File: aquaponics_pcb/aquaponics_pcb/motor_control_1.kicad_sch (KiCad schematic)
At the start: 1 part, among them IC4 DRV8214RTER

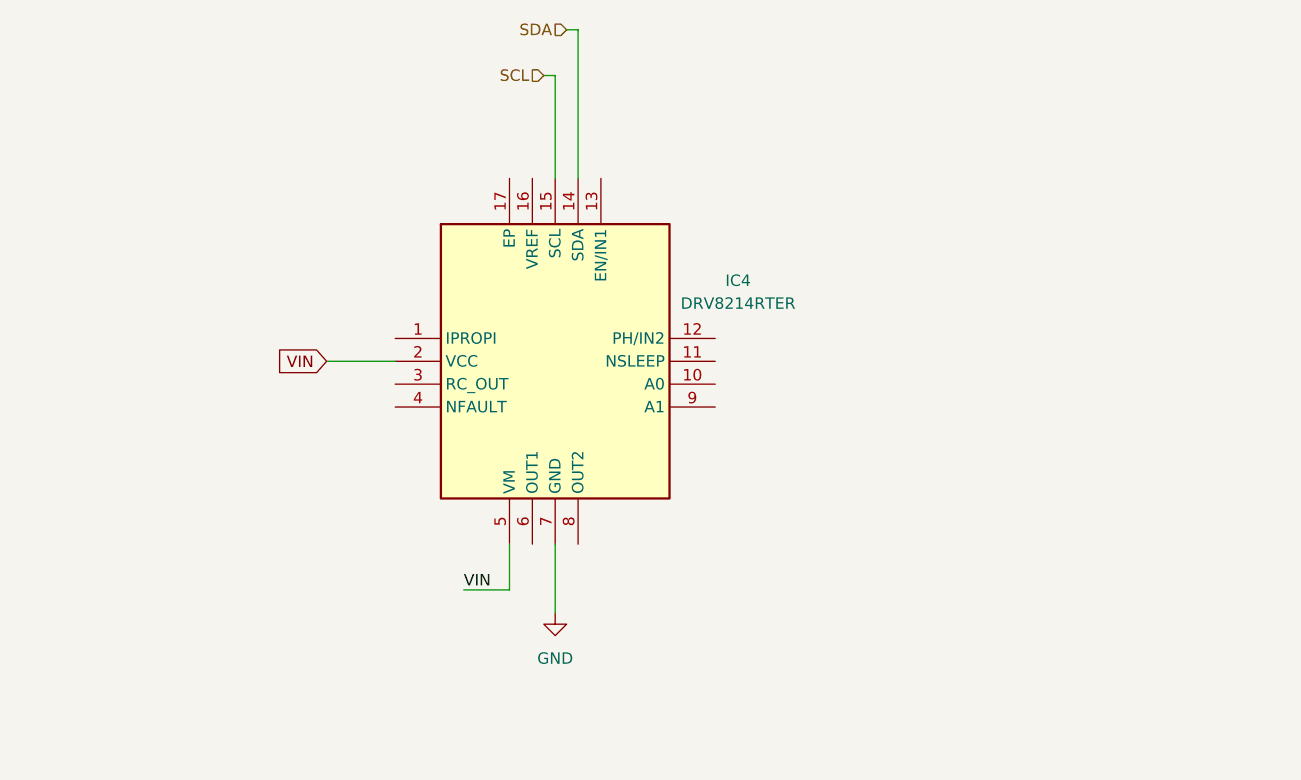
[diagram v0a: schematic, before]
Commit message: add ezo datasheets, update motor schematic and add 2 motors
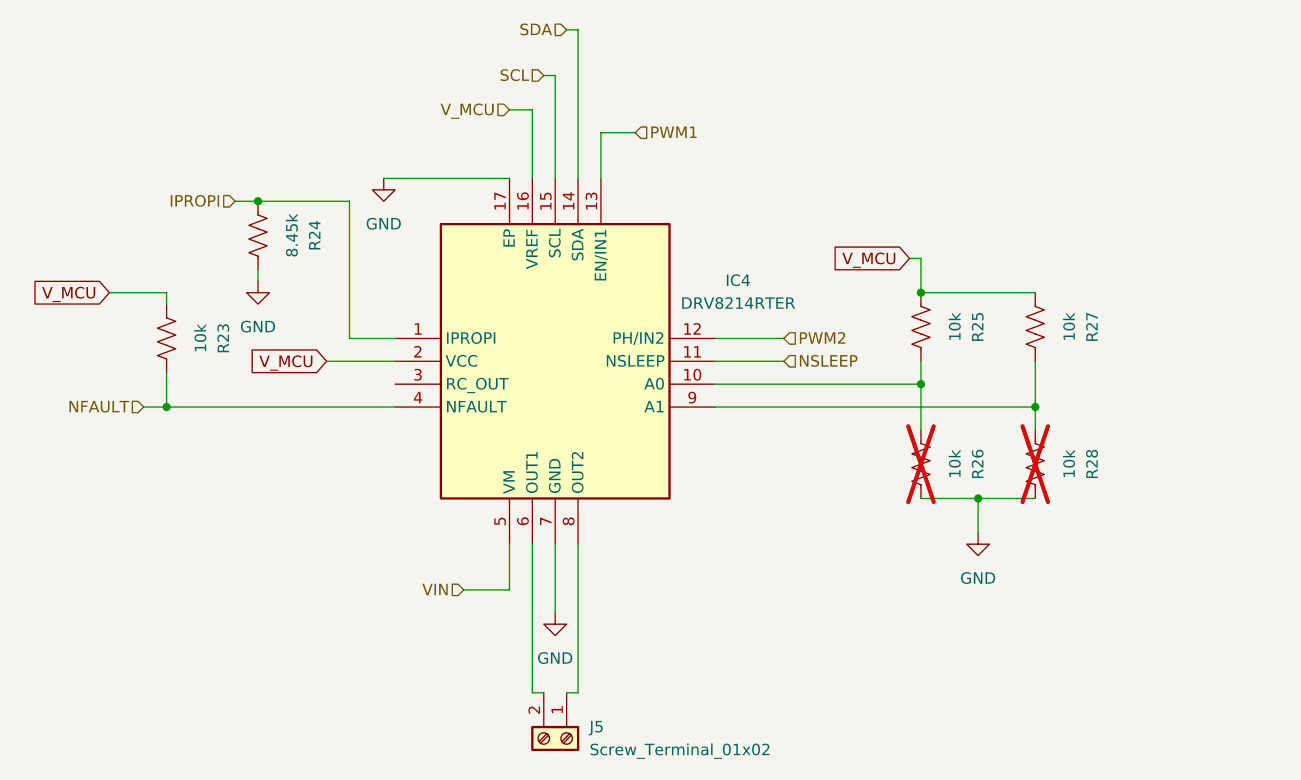
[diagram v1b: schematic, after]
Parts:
- added J5: Screw_Terminal_01x02, symbol Connector:Screw_Terminal_01x02
- added R23, R25, R26, R27, R28: 10k, Resistor_SMD:R_0603_1608Metric_Pad0.98x0.95mm_HandSolder, symbol Device:R_US
- added R24: 8.45k, Resistor_SMD:R_0603_1608Metric_Pad0.98x0.95mm_HandSolder, symbol Device:R_US
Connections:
- net GND: now also IC4.17 (EP), R24.2, R26.2, R28.2
- net VIN: no longer IC4.2 (VCC)
- net IPROPI: now reaches IC4.1 (IPROPI)
- net IPROPI: now also R24.1
- net at IC4.10 (A0): now also R25.2, R26.1
- net NSLEEP: now reaches IC4.11 (NSLEEP)
- net PWM2: now reaches IC4.12 (PH/IN2)
- net PWM1: now reaches IC4.13 (EN/IN1)
- net V_MCU: now reaches IC4.16 (VREF)
- net V_MCU: now also IC4.2 (VCC), R23.1, R25.1, R27.1
- net NFAULT: now reaches IC4.4 (NFAULT)
- net NFAULT: now also R23.2
- net at IC4.6 (OUT1): now also J5.2 (Pin_2)
- net at IC4.8 (OUT2): now also J5.1 (Pin_1)
- net at IC4.9 (A1): now also R27.2, R28.1

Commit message: add initial pcb layout
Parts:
- IC4: footprint QFN50P300X300X80-17N-D -> SamacSys_Parts:QFN50P300X300X80-17N-D
- J5: footprint (none) -> Connector_Phoenix_GMSTB:PhoenixContact_GMSTBA_2,5_2-G_1x02_P7.50mm_Horizontal
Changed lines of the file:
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@@
 			)
 		)
-		(property "Footprint" "QFN50P300X300X80-17N-D"
+		(property "Footprint" "SamacSys_Parts:QFN50P300X300X80-17N-D"
 			(at 153.67 171.12 0)
 			(effects
@@
 			)
 		)
-		(property "Footprint" ""
+		(property "Footprint" "Connector_Phoenix_GMSTB:PhoenixContact_GMSTBA_2,5_2-G_1x02_P7.50mm_Horizontal"
 			(at 140.97 130.81 0)
 			(effects

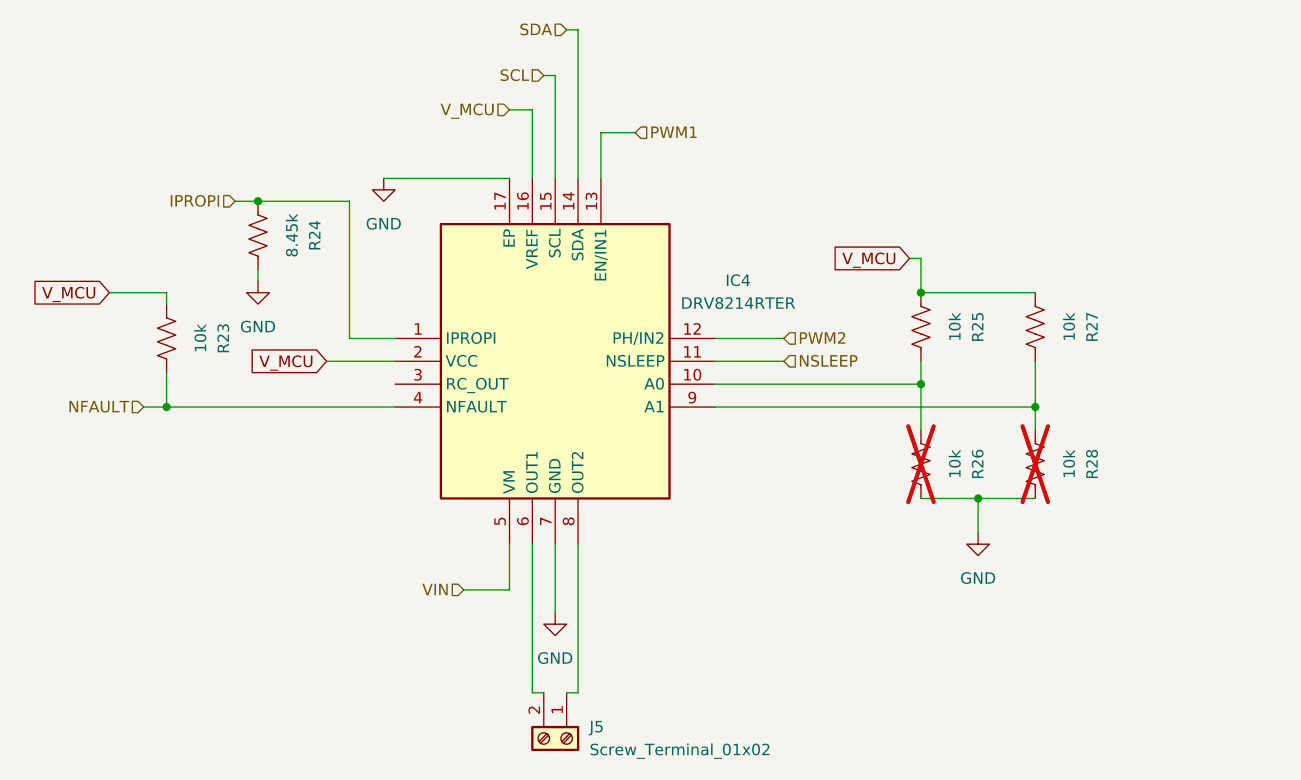
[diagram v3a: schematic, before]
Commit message: finish ground and power pours. fix rules and run final DRC. export gerbers
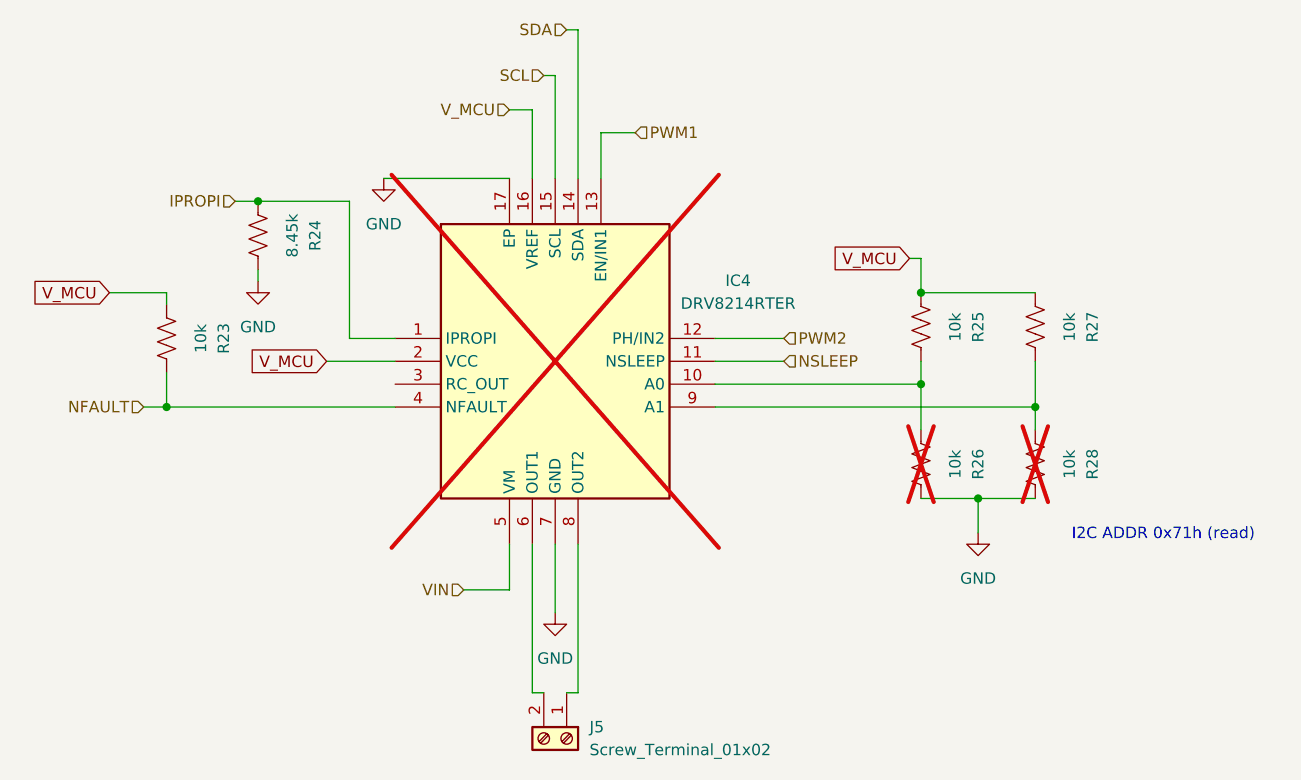
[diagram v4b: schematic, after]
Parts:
- IC4: now not fitted
- R23, R25, R27: JLCPCB Part # (none) -> C98220; LCSC Part Number (none) -> C98220
- R24: JLCPCB Part # (none) -> C2933263; LCSC Part Number (none) -> C2933263
- R26, R28: LCSC Part Number (none) -> C98220
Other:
- note added: "I2C ADDR 0x71h (read)"
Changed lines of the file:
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@@
 	(generator_version "9.0")
 	(paper "A4")
+	(text "I2C ADDR 0x71h (read)"
+		(exclude_from_sim no)
+		(at 207.264 108.204 0)
+		(effects
+			(font
+				(size 1.27 1.27)
+			)
+		)
+	)
 	(junction
 		(at 180.34 81.28)
@@
 		(property "Description" "Resistor, US symbol"
 			(at 180.34 85.09 0)
+			(effects
+				(font
+					(size 1.27 1.27)
+				)
+				(hide yes)
+			)
+		)
+		(property "LCSC Part Number" "C98220"
+			(at 180.34 85.09 90)
+			(effects
+				(font
+					(size 1.27 1.27)
+				)
+				(hide yes)
+			)
+		)
+		(property "JLCPCB Part #" "C98220"
+			(at 180.34 85.09 90)
 			(effects
 				(font
@@
 			)
 		)
+		(property "LCSC Part Number" "C98220"
+			(at 193.04 85.09 90)
+			(effects
+				(font
+					(size 1.27 1.27)
+				)
+				(hide yes)
+			)
+		)
+		(property "JLCPCB Part #" "C98220"
+			(at 193.04 85.09 90)
+			(effects
+				(font
+					(size 1.27 1.27)
+				)
+				(hide yes)
+			)
+		)
 		(pin "1"
 		)
@@
 			)
 		)
+		(property "LCSC Part Number" "C98220"
+			(at 180.34 100.33 90)
+			(effects
+				(font
+					(size 1.27 1.27)
+				)
+				(hide yes)
+			)
+		)
+		(property "JLCPCB Part #" ""
+			(at 180.34 100.33 90)
+			(effects
+				(font
+					(size 1.27 1.27)
+				)
+				(hide yes)
+			)
+		)
 		(pin "1"
 		)
@@
 			)
 		)
+		(property "LCSC Part Number" "C98220"
+			(at 193.04 100.33 90)
+			(effects
+				(font
+					(size 1.27 1.27)
+				)
+				(hide yes)
+			)
+		)
+		(property "JLCPCB Part #" ""
+			(at 193.04 100.33 90)
+			(effects
+				(font
+					(size 1.27 1.27)
+				)
+				(hide yes)
+			)
+		)
 		(pin "1"
 		)
@@
 			)
 		)
+		(property "LCSC Part Number" "C98220"
+			(at 96.52 86.36 90)
+			(effects
+				(font
+					(size 1.27 1.27)
+				)
+				(hide yes)
+			)
+		)
+		(property "JLCPCB Part #" "C98220"
+			(at 96.52 86.36 90)
+			(effects
+				(font
+					(size 1.27 1.27)
+				)
+				(hide yes)
+			)
+		)
 		(pin "1"
 		)
@@
 		(property "Description" "Resistor, US symbol"
 			(at 106.68 74.93 0)
+			(effects
+				(font
+					(size 1.27 1.27)
+				)
+				(hide yes)
+			)
+		)
+		(property "LCSC Part Number" "C2933263"
+			(at 106.68 74.93 90)
+			(effects
+				(font
+					(size 1.27 1.27)
+				)
+				(hide yes)
+			)
+		)
+		(property "JLCPCB Part #" "C2933263"
+			(at 106.68 74.93 90)
 			(effects
 				(font
@@
 		(in_bom yes)
 		(on_board yes)
-		(dnp no)
+		(dnp yes)
 		(fields_autoplaced yes)
 		(property "Reference" "IC4"
@@
 				)
 				(justify left top)
+				(hide yes)
+			)
+		)
+		(property "LCSC Part Number" ""
+			(at 121.92 86.36 0)
+			(effects
+				(font
+					(size 1.27 1.27)
+				)
+				(hide yes)
+			)
+		)
+		(property "JLCPCB Part #" ""
+			(at 121.92 86.36 0)
+			(effects
+				(font
+					(size 1.27 1.27)
+				)
 				(hide yes)
 			)
@@
 			(effects
 				(font
+					(size 1.27 1.27)
+				)
+				(hide yes)
+			)
+		)
+		(property "LCSC Part Number" ""
+			(at 140.97 130.81 90)
+			(effects
+				(font
+					(size 1.27 1.27)
+				)
+				(hide yes)
+			)
+		)
+		(property "JLCPCB Part #" ""
+			(at 140.97 130.81 90)
+			(effects
+				(font
